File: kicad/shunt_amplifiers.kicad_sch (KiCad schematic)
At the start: 44 parts, among them Q2 IRF7749L1, Q3 IRF7749L1, Q4 IRF7749L1, Q5 IRF7749L1, Q6 IRF7749L1, Q7 IRF7749L1, U10 AD8418, U11 SN74LVC1G66DCKR, U12 SN74LVC1G66DCKR, U13 SN74LVC1G66DCKR, U8 AD8418, U9 AD8418

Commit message: checking shunt footprints
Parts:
- R34: renamed from R16; footprint Resistor_SMD:R_Shunt_Isabellenhuette_BVR4026 -> Resistor_SMD:R_Shunt_Vishay_WSR2_WSR3
- renumbered C36 to C38, C37 to C39, C39 to C40, C40 to C41, C35 to C44, C38 to C45, C41 to C46, C44 to C47, C47 to C48, C45 to C50, C46 to C51, C48 to C52, Q2 to Q1, Q4 to Q2, Q6 to Q3, Q3 to Q4, Q7 to Q6, R17 to R31, R20 to R32, R23 to R33, R19 to R35, R22 to R36, R18 to R37, R21 to R38, R24 to R39, R25 to R40, R26 to R41, R27 to R42, TP2 to TP3, TP1 to TP4, TP4 to TP5, TP5 to TP6, TP3 to TP7

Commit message: working on fet fp
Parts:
- Q1, Q2, Q3, Q4, Q5, Q6: footprint Package_DirectFET:DirectFET_L6 -> footprints:TRANS_BSC014N04LSIATMA1; symbol Transistor_FET:IRF7748L1 -> Transistor_FET:BSC123N08NS3G
- R34: footprint Resistor_SMD:R_Shunt_Vishay_WSR2_WSR3 -> footprints:RESC10052X105N
- R35, R36: footprint Resistor_SMD:R_Shunt_Isabellenhuette_BVR4026 -> footprints:RESC10052X105N
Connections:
- net GND: now also Q4.1 (S), Q4.2 (S), Q4.3 (S), Q5.1 (S), Q5.2 (S), Q5.3 (S), Q6.1 (S), Q6.2 (S), Q6.3 (S); no longer Q4.S, Q5.S, Q6.S
- net SH_A: now also Q1.1 (S), Q1.2 (S), Q1.3 (S), Q4.5 (D); no longer Q1.S, Q4.D
- net SH_B: now also Q2.1 (S), Q2.2 (S), Q2.3 (S), Q5.5 (D); no longer Q2.S, Q5.D
- net SH_C: now also Q3.1 (S), Q3.2 (S), Q3.3 (S), Q6.5 (D); no longer Q3.S, Q6.D
- net SUPPLY: now also Q1.5 (D), Q2.5 (D), Q3.5 (D); no longer Q1.D, Q2.D, Q3.D
- net at R31.2: now also Q1.4 (G); no longer Q1.G
- net at R37.2: now also Q4.4 (G); no longer Q4.G
- net at R39.2: now also Q6.4 (G); no longer Q6.G
- net at R33.2: now also Q3.4 (G); no longer Q3.G
- net at R38.2: now also Q5.4 (G); no longer Q5.G
- net at R32.2: now also Q2.4 (G); no longer Q2.G
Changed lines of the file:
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@@
 	)
 	(symbol
-		(lib_id "Transistor_FET:IRF7748L1")
+		(lib_id "Transistor_FET:BSC123N08NS3G")
 		(at 87.63 46.99 0)
 		(unit 1)
@@
 			)
 		)
-		(property "Footprint" "Package_DirectFET:DirectFET_L6"
+		(property "Footprint" "footprints:TRANS_BSC014N04LSIATMA1"
 			(at 92.71 48.895 0)
 			(effects
@@
 			)
 		)
-		(property "Datasheet" ""
+		(property "Datasheet" "http://www.infineon.com/dgdl/Infineon-BSC123N08NS3G-DS-v02_05-en.pdf?fileId=db3a30431add1d95011ae80eb8555625"
 			(at 92.71 50.8 0)
 			(effects
@@
 			)
 		)
-		(property "Description" ""
+		(property "Description" "55A Id, 80V Vds, OptiMOS N-Channel Power MOSFET, 12.3mOhm Ron, Qg (typ) 19.0nC, PG-TDSON-8"
 			(at 87.63 46.99 0)
 			(effects
@@
 			)
 		)
-		(pin "G"
+		(pin "2"
+		)
+		(pin "5"
+		)
+		(pin "4"
 		)
-		(pin "S"
+		(pin "3"
 		)
-		(pin "D"
+		(pin "1"
 		)
 		(instances
@@
 	)
 	(symbol
-		(lib_id "Transistor_FET:IRF7748L1")
+		(lib_id "Transistor_FET:BSC123N08NS3G")
 		(at 87.63 74.93 0)
 		(unit 1)
@@
 			)
 		)
-		(property "Footprint" "Package_DirectFET:DirectFET_L6"
+		(property "Footprint" "footprints:TRANS_BSC014N04LSIATMA1"
 			(at 92.71 76.835 0)
 			(effects
@@
 			)
 		)
-		(property "Datasheet" ""
+		(property "Datasheet" "http://www.infineon.com/dgdl/Infineon-BSC123N08NS3G-DS-v02_05-en.pdf?fileId=db3a30431add1d95011ae80eb8555625"
 			(at 92.71 78.74 0)
 			(effects
@@
 			)
 		)
-		(property "Description" ""
+		(property "Description" "55A Id, 80V Vds, OptiMOS N-Channel Power MOSFET, 12.3mOhm Ron, Qg (typ) 19.0nC, PG-TDSON-8"
 			(at 87.63 74.93 0)
 			(effects
@@
 			)
 		)
-		(pin "G"
+		(pin "4"
 		)
-		(pin "S"
+		(pin "5"
 		)
-		(pin "D"
+		(pin "2"
+		)
+		(pin "3"
+		)
+		(pin "1"
 		)
 		(instances
@@
 	)
 	(symbol
-		(lib_id "Transistor_FET:IRF7748L1")
+		(lib_id "Transistor_FET:BSC123N08NS3G")
 		(at 241.3 74.93 0)
 		(unit 1)
@@
 			)
 		)
-		(property "Footprint" "Package_DirectFET:DirectFET_L6"
+		(property "Footprint" "footprints:TRANS_BSC014N04LSIATMA1"
 			(at 246.38 76.835 0)
 			(effects
@@
 			)
 		)
-		(property "Datasheet" ""
+		(property "Datasheet" "http://www.infineon.com/dgdl/Infineon-BSC123N08NS3G-DS-v02_05-en.pdf?fileId=db3a30431add1d95011ae80eb8555625"
 			(at 246.38 78.74 0)
 			(effects
@@
 			)
 		)
-		(property "Description" ""
+		(property "Description" "55A Id, 80V Vds, OptiMOS N-Channel Power MOSFET, 12.3mOhm Ron, Qg (typ) 19.0nC, PG-TDSON-8"
 			(at 241.3 74.93 0)
 			(effects
@@
 			)
 		)
-		(pin "G"
+		(pin "2"
 		)
-		(pin "S"
+		(pin "5"
+		)
+		(pin "4"
 		)
-		(pin "D"
+		(pin "1"
+		)
+		(pin "3"
 		)
 		(instances
@@
 			)
 		)
-		(property "Footprint" "Resistor_SMD:R_Shunt_Isabellenhuette_BVR4026"
+		(property "Footprint" "footprints:RESC10052X105N"
 			(at 128.27 52.832 90)
 			(effects
@@
 	)
 	(symbol
-		(lib_id "Transistor_FET:IRF7748L1")
+		(lib_id "Transistor_FET:BSC123N08NS3G")
 		(at 165.1 74.93 0)
 		(unit 1)
@@
 			)
 		)
-		(property "Footprint" "Package_DirectFET:DirectFET_L6"
+		(property "Footprint" "footprints:TRANS_BSC014N04LSIATMA1"
 			(at 170.18 76.835 0)
 			(effects
@@
 			)
 		)
-		(property "Datasheet" ""
+		(property "Datasheet" "http://www.infineon.com/dgdl/Infineon-BSC123N08NS3G-DS-v02_05-en.pdf?fileId=db3a30431add1d95011ae80eb8555625"
 			(at 170.18 78.74 0)
 			(effects
@@
 			)
 		)
-		(property "Description" ""
+		(property "Description" "55A Id, 80V Vds, OptiMOS N-Channel Power MOSFET, 12.3mOhm Ron, Qg (typ) 19.0nC, PG-TDSON-8"
 			(at 165.1 74.93 0)
 			(effects
@@
 			)
 		)
-		(pin "G"
+		(pin "4"
+		)
+		(pin "5"
+		)
+		(pin "2"
 		)
-		(pin "S"
+		(pin "3"
 		)
-		(pin "D"
+		(pin "1"
 		)
 		(instances
@@
 	)
 	(symbol
-		(lib_id "Transistor_FET:IRF7748L1")
+		(lib_id "Transistor_FET:BSC123N08NS3G")
 		(at 241.3 46.99 0)
 		(unit 1)
@@
 			)
 		)
-		(property "Footprint" "Package_DirectFET:DirectFET_L6"
+		(property "Footprint" "footprints:TRANS_BSC014N04LSIATMA1"
 			(at 246.38 48.895 0)
 			(effects
@@
 			)
 		)
-		(property "Datasheet" ""
+		(property "Datasheet" "http://www.infineon.com/dgdl/Infineon-BSC123N08NS3G-DS-v02_05-en.pdf?fileId=db3a30431add1d95011ae80eb8555625"
 			(at 246.38 50.8 0)
 			(effects
@@
 			)
 		)
-		(property "Description" ""
+		(property "Description" "55A Id, 80V Vds, OptiMOS N-Channel Power MOSFET, 12.3mOhm Ron, Qg (typ) 19.0nC, PG-TDSON-8"
 			(at 241.3 46.99 0)
 			(effects
@@
 			)
 		)
-		(pin "G"
+		(pin "4"
 		)
-		(pin "S"
+		(pin "1"
 		)
-		(pin "D"
+		(pin "5"
+		)
+		(pin "2"
+		)
+		(pin "3"
 		)
 		(instances
@@
 			)
 		)
-		(property "Footprint" "Resistor_SMD:R_Shunt_Isabellenhuette_BVR4026"
+		(property "Footprint" "footprints:RESC10052X105N"
 			(at 204.47 52.832 90)
 			(effects
@@
 	)
 	(symbol
-		(lib_id "Transistor_FET:IRF7748L1")
+		(lib_id "Transistor_FET:BSC123N08NS3G")
 		(at 165.1 46.99 0)
 		(unit 1)
@@
 			)
 		)
-		(property "Footprint" "Package_DirectFET:DirectFET_L6"
+		(property "Footprint" "footprints:TRANS_BSC014N04LSIATMA1"
 			(at 170.18 48.895 0)
 			(effects
@@
 			)
 		)
-		(property "Datasheet" ""
+		(property "Datasheet" "http://www.infineon.com/dgdl/Infineon-BSC123N08NS3G-DS-v02_05-en.pdf?fileId=db3a30431add1d95011ae80eb8555625"
 			(at 170.18 50.8 0)
 			(effects
@@
 			)
 		)
-		(property "Description" ""
+		(property "Description" "55A Id, 80V Vds, OptiMOS N-Channel Power MOSFET, 12.3mOhm Ron, Qg (typ) 19.0nC, PG-TDSON-8"
 			(at 165.1 46.99 0)
 			(effects
@@
 			)
 		)
-		(pin "G"
+		(pin "3"
 		)
-		(pin "S"
+		(pin "5"
+		)
+		(pin "4"
 		)
-		(pin "D"
+		(pin "1"
+		)
+		(pin "2"
 		)
 		(instances
@@
 			)
 		)
-		(property "Footprint" "Resistor_SMD:R_Shunt_Vishay_WSR2_WSR3"
+		(property "Footprint" "footprints:RESC10052X105N"
 			(at 50.8 52.832 90)
 			(effects

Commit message: routing gate driver
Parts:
- Q1, Q2, Q3, Q4, Q5, Q6: footprint footprints:TRANS_BSC014N04LSIATMA1 -> footprints:TRANS_BSC014N04LSIATMA1_Custom; symbol Transistor_FET:BSC123N08NS3G -> custom:BSC014N06NS
- TP3, TP4, TP5, TP6, TP7: footprint TestPoint:TestPoint_Pad_4.0x4.0mm -> footprints:TestPoint_Pad_5.5x4.0mm
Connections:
- net GND: now also Q4.S, Q5.S, Q6.S; no longer Q4.1 (S), Q5.1 (S), Q6.1 (S)
- net SH_A: now also Q1.S, Q4.D; no longer Q1.1 (S), Q4.5 (D)
- net SH_B: now also Q2.S, Q5.D; no longer Q2.1 (S), Q5.5 (D)
- net SH_C: now also Q3.S, Q6.D; no longer Q3.1 (S), Q6.5 (D)
- net SUPPLY: now also Q1.D, Q2.D, Q3.D; no longer Q1.5 (D), Q2.5 (D), Q3.5 (D)
- net at R31.2: now also Q1.G; no longer Q1.4 (G)
- net at R37.2: now also Q4.G; no longer Q4.4 (G)
- net at R39.2: now also Q6.G; no longer Q6.4 (G)
- net at R33.2: now also Q3.G; no longer Q3.4 (G)
- net at R38.2: now also Q5.G; no longer Q5.4 (G)
- net at R32.2: now also Q2.G; no longer Q2.4 (G)
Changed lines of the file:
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@@
 		(title "rESC")
 		(date "2025-05-24")
-		(rev "a")
+		(rev "1")
 		(company "Tyler Lindsay")
 	)
@@
 	)
 	(symbol
-		(lib_id "Transistor_FET:BSC123N08NS3G")
+		(lib_id "custom:BSC014N06NS")
 		(at 87.63 46.99 0)
 		(unit 1)
@@
 				)
 				(justify left)
+				(hide yes)
 			)
 		)
-		(property "Footprint" "footprints:TRANS_BSC014N04LSIATMA1"
+		(property "Footprint" "footprints:TRANS_BSC014N04LSIATMA1_Custom"
 			(at 92.71 48.895 0)
 			(effects
@@
 		(pin "2"
 		)
-		(pin "5"
+		(pin "D"
 		)
-		(pin "4"
+		(pin "G"
 		)
 		(pin "3"
 		)
-		(pin "1"
+		(pin "S"
 		)
 		(instances
@@
 	)
 	(symbol
-		(lib_id "Transistor_FET:BSC123N08NS3G")
+		(lib_id "custom:BSC014N06NS")
 		(at 87.63 74.93 0)
 		(unit 1)
@@
 				)
 				(justify left)
+				(hide yes)
 			)
 		)
-		(property "Footprint" "footprints:TRANS_BSC014N04LSIATMA1"
+		(property "Footprint" "footprints:TRANS_BSC014N04LSIATMA1_Custom"
 			(at 92.71 76.835 0)
 			(effects
@@
 			)
 		)
-		(pin "4"
+		(pin "S"
 		)
-		(pin "5"
+		(pin "G"
 		)
 		(pin "2"
@@
 		(pin "3"
 		)
-		(pin "1"
+		(pin "D"
 		)
 		(instances
@@
 	)
 	(symbol
-		(lib_id "Transistor_FET:BSC123N08NS3G")
+		(lib_id "custom:BSC014N06NS")
 		(at 241.3 74.93 0)
 		(unit 1)
@@
 				)
 				(justify left)
+				(hide yes)
 			)
 		)
-		(property "Footprint" "footprints:TRANS_BSC014N04LSIATMA1"
+		(property "Footprint" "footprints:TRANS_BSC014N04LSIATMA1_Custom"
 			(at 246.38 76.835 0)
 			(effects
@@
 		(pin "2"
 		)
-		(pin "5"
+		(pin "G"
 		)
-		(pin "4"
+		(pin "S"
 		)
-		(pin "1"
+		(pin "D"
 		)
 		(pin "3"
@@
 			)
 		)
-		(property "Footprint" "TestPoint:TestPoint_Pad_4.0x4.0mm"
+		(property "Footprint" "footprints:TestPoint_Pad_5.5x4.0mm"
 			(at 64.77 97.79 0)
 			(effects
@@
 			)
 		)
-		(property "Footprint" "TestPoint:TestPoint_Pad_4.0x4.0mm"
+		(property "Footprint" "footprints:TestPoint_Pad_5.5x4.0mm"
 			(at 36.83 49.53 0)
 			(effects
@@
 			)
 		)
-		(property "Footprint" "TestPoint:TestPoint_Pad_4.0x4.0mm"
+		(property "Footprint" "footprints:TestPoint_Pad_5.5x4.0mm"
 			(at 40.64 27.94 0)
 			(effects
@@
 	)
 	(symbol
-		(lib_id "Transistor_FET:BSC123N08NS3G")
+		(lib_id "custom:BSC014N06NS")
 		(at 165.1 74.93 0)
 		(unit 1)
@@
 				)
 				(justify left)
+				(hide yes)
 			)
 		)
-		(property "Footprint" "footprints:TRANS_BSC014N04LSIATMA1"
+		(property "Footprint" "footprints:TRANS_BSC014N04LSIATMA1_Custom"
 			(at 170.18 76.835 0)
 			(effects
@@
 			)
 		)
-		(pin "4"
+		(pin "G"
 		)
-		(pin "5"
+		(pin "S"
 		)
 		(pin "2"
@@
 		(pin "3"
 		)
-		(pin "1"
+		(pin "D"
 		)
 		(instances
@@
 	)
 	(symbol
-		(lib_id "Transistor_FET:BSC123N08NS3G")
+		(lib_id "custom:BSC014N06NS")
 		(at 241.3 46.99 0)
 		(unit 1)
@@
 				)
 				(justify left)
+				(hide yes)
 			)
 		)
-		(property "Footprint" "footprints:TRANS_BSC014N04LSIATMA1"
+		(property "Footprint" "footprints:TRANS_BSC014N04LSIATMA1_Custom"
 			(at 246.38 48.895 0)
 			(effects
@@
 			)
 		)
-		(pin "4"
+		(pin "D"
 		)
-		(pin "1"
+		(pin "G"
 		)
-		(pin "5"
+		(pin "S"
 		)
 		(pin "2"
@@
 			)
 		)
-		(property "Footprint" "TestPoint:TestPoint_Pad_4.0x4.0mm"
+		(property "Footprint" "footprints:TestPoint_Pad_5.5x4.0mm"
 			(at 118.11 49.53 0)
 			(effects
@@
 			)
 		)
-		(property "Footprint" "TestPoint:TestPoint_Pad_4.0x4.0mm"
+		(property "Footprint" "footprints:TestPoint_Pad_5.5x4.0mm"
 			(at 194.31 49.53 0)
 			(effects
@@
 	)
 	(symbol
-		(lib_id "Transistor_FET:BSC123N08NS3G")
+		(lib_id "custom:BSC014N06NS")
 		(at 165.1 46.99 0)
 		(unit 1)
@@
 				)
 				(justify left)
+				(hide yes)
 			)
 		)
-		(property "Footprint" "footprints:TRANS_BSC014N04LSIATMA1"
+		(property "Footprint" "footprints:TRANS_BSC014N04LSIATMA1_Custom"
 			(at 170.18 48.895 0)
 			(effects
@@
 		(pin "3"
 		)
-		(pin "5"
+		(pin "S"
 		)
-		(pin "4"
+		(pin "G"
 		)
-		(pin "1"
+		(pin "D"
 		)
 		(pin "2"

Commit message: done? without test points
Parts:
- Q1, Q2, Q3, Q4, Q5, Q6: footprint footprints:TRANS_BSC014N04LSIATMA1_Custom -> footprints:TRANS_BSC014N04LSIATMA1_Custom_NoSilkscreen
- U11, U12, U13: footprint footprints:SOT65P210X110-5N -> footprints:SOT65P210X110-5N_Custom
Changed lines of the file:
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@@
 			)
 		)
-		(property "Footprint" "footprints:TRANS_BSC014N04LSIATMA1_Custom"
+		(property "Footprint" "footprints:TRANS_BSC014N04LSIATMA1_Custom_NoSilkscreen"
 			(at 92.71 48.895 0)
 			(effects
@@
 			)
 		)
-		(property "Footprint" "footprints:TRANS_BSC014N04LSIATMA1_Custom"
+		(property "Footprint" "footprints:TRANS_BSC014N04LSIATMA1_Custom_NoSilkscreen"
 			(at 92.71 76.835 0)
 			(effects
@@
 			)
 		)
-		(property "Footprint" "footprints:SOT65P210X110-5N"
+		(property "Footprint" "footprints:SOT65P210X110-5N_Custom"
 			(at 209.804 137.922 0)
 			(effects
@@
 			)
 		)
-		(property "Footprint" "footprints:TRANS_BSC014N04LSIATMA1_Custom"
+		(property "Footprint" "footprints:TRANS_BSC014N04LSIATMA1_Custom_NoSilkscreen"
 			(at 246.38 76.835 0)
 			(effects
@@
 			)
 		)
-		(property "Footprint" "footprints:SOT65P210X110-5N"
+		(property "Footprint" "footprints:SOT65P210X110-5N_Custom"
 			(at 56.134 137.922 0)
 			(effects
@@
 			)
 		)
-		(property "Footprint" "footprints:TRANS_BSC014N04LSIATMA1_Custom"
+		(property "Footprint" "footprints:TRANS_BSC014N04LSIATMA1_Custom_NoSilkscreen"
 			(at 170.18 76.835 0)
 			(effects
@@
 			)
 		)
-		(property "Footprint" "footprints:TRANS_BSC014N04LSIATMA1_Custom"
+		(property "Footprint" "footprints:TRANS_BSC014N04LSIATMA1_Custom_NoSilkscreen"
 			(at 246.38 48.895 0)
 			(effects
@@
 			)
 		)
-		(property "Footprint" "footprints:SOT65P210X110-5N"
+		(property "Footprint" "footprints:SOT65P210X110-5N_Custom"
 			(at 133.604 137.922 0)
 			(effects
@@
 			)
 		)
-		(property "Footprint" "footprints:TRANS_BSC014N04LSIATMA1_Custom"
+		(property "Footprint" "footprints:TRANS_BSC014N04LSIATMA1_Custom_NoSilkscreen"
 			(at 170.18 48.895 0)
 			(effects

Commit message: revert to v6.05
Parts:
- removed R31, R32, R33, R37, R38, R39: 4.7R, Resistor_SMD:R_0402_1005Metric, symbol Device:R
- added NT1, NT2, NT3: NetTie_2, NetTie:NetTie-2_SMD_Pad0.5mm, symbol Device:NetTie_2
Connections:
- net GH_A: now also Q1.G
- net GH_B: now also Q2.G
- net GH_C: now also Q3.G
- net GL_A: now also Q4.G
- net GL_B: now also Q5.G
- net GL_C: now also Q6.G
- net GND: now also NT1.2, NT2.2, NT3.2
- new net SL_A: NT1.1
- new net SL_B: NT2.1
- new net SL_C: NT3.1

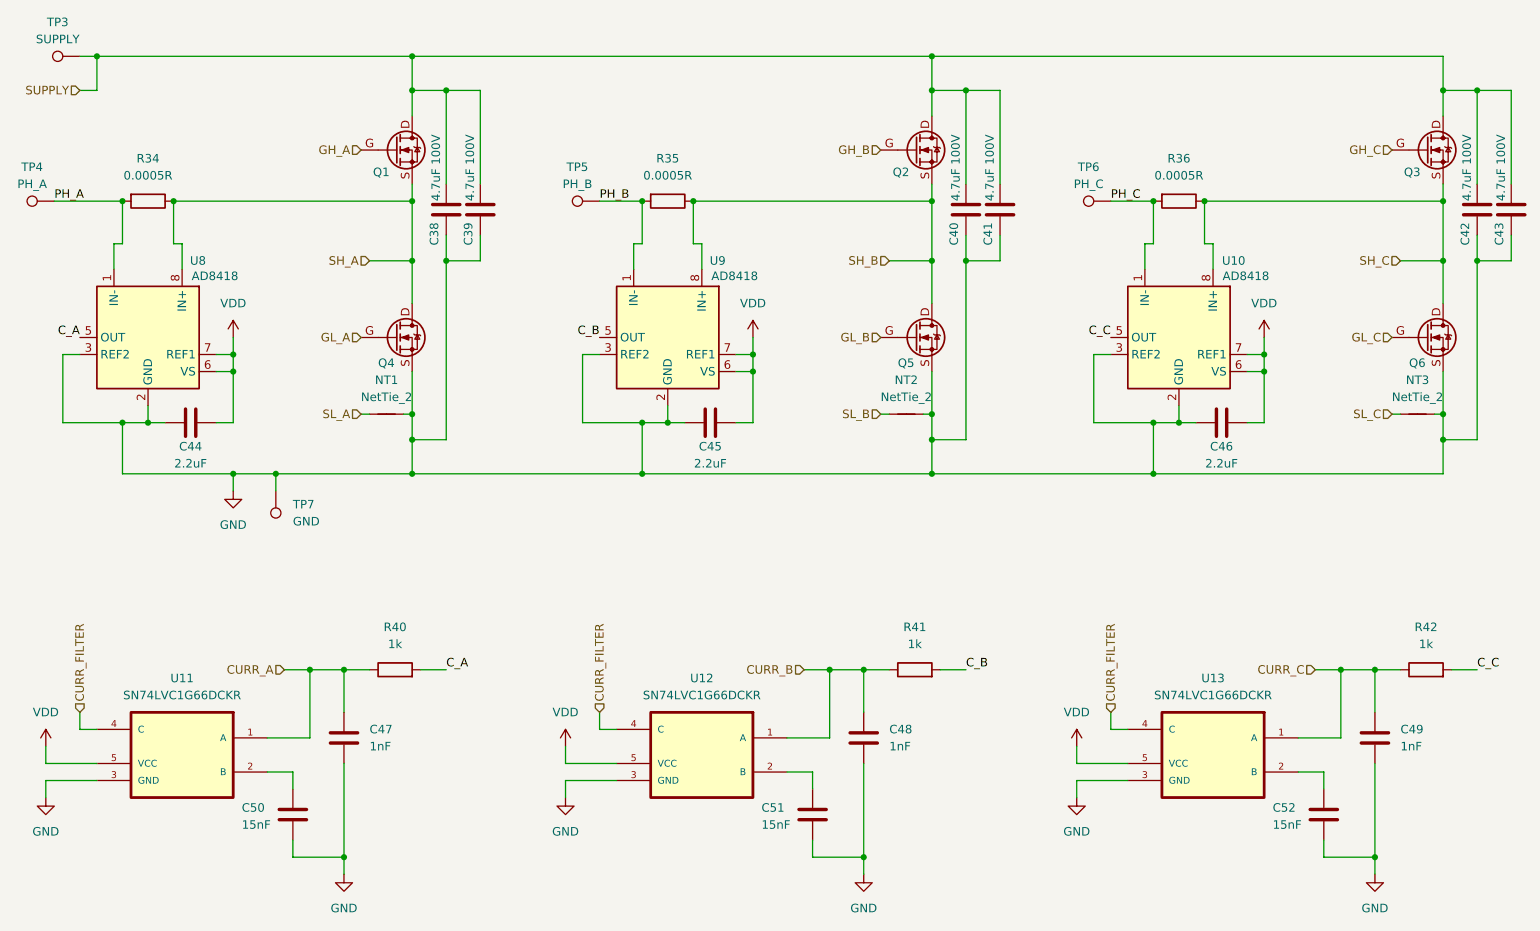
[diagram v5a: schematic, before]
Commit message: gate driver mostly schematic'd and pcb started
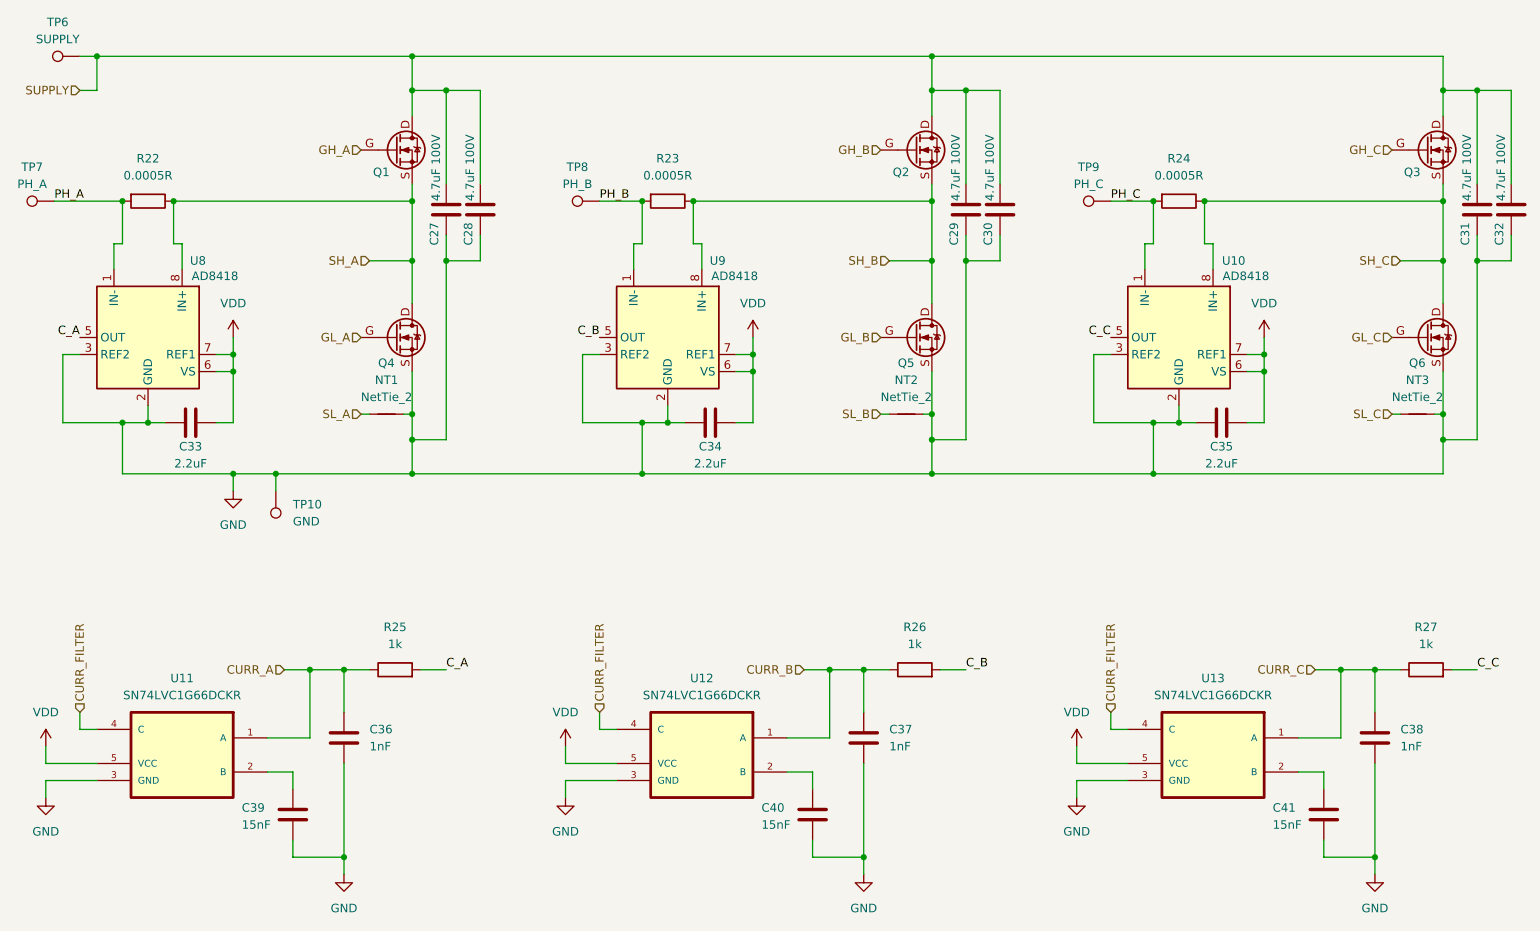
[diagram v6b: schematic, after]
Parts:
- renumbered C38 to C27, C39 to C28, C40 to C29, C41 to C30, C42 to C31, C43 to C32, C44 to C33, C45 to C34, C46 to C35, C47 to C36, C48 to C37, C49 to C38, C50 to C39, C51 to C40, C52 to C41, R34 to R22, R35 to R23, R36 to R24, R40 to R25, R41 to R26, R42 to R27, TP7 to TP10, TP3 to TP6, TP4 to TP7, TP5 to TP8, TP6 to TP9

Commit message: rev3 ordered
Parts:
- NT1, NT2, NT3: footprint NetTie:NetTie-2_SMD_Pad0.5mm -> footprints:NetTie-2_SMD_Pad0.2mm
- R34: renamed from R22; symbol Device:R -> Device:R_US
- R35: renamed from R23; symbol Device:R -> Device:R_US
- R36: renamed from R24; symbol Device:R -> Device:R_US
- R40: renamed from R25; symbol Device:R -> Device:R_US
- R41: renamed from R26; symbol Device:R -> Device:R_US
- R42: renamed from R27; symbol Device:R -> Device:R_US
- renumbered C27 to C38, C28 to C39, C29 to C40, C30 to C41, C31 to C42, C32 to C43, C33 to C44, C34 to C45, C35 to C46, C36 to C47, C37 to C48, C38 to C49, C39 to C50, C40 to C51, C41 to C52, TP6 to TP3, TP7 to TP4, TP8 to TP5, TP9 to TP6, TP10 to TP7
